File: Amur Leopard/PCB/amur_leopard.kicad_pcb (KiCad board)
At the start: 2 copper layers, 110.3 x 38.1 mm, 32 parts, among them SW1 SW_Push, U1 ATmega32U4-AU, Y1 16MHz

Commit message: Improve Amur Leopard-PCB
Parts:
- moved USB1 28.3 mm to (151.6, 109.5), turned to 0 degrees
- moved R3 24.8 mm to (161.3, 111.6), turned to 270 degrees
- moved R2 21.2 mm to (159.4, 109.7), turned to 270 degrees
- moved C3 1.75 mm to (153.8, 96.0), turned to 270 degrees
- moved C7 0.13 mm to (165.1, 109.4)
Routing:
- net VCC: track 39.0 -> 18.5 mm
- net GND: track 142.3 -> 133.6 mm
- net Net-(C3-Pad1): track 5.98 -> 8.94 mm
- net Net-(R1-Pad2): track 56.4 -> 53.8 mm
- net D-: track 3.88 -> 6.10 mm
- net Net-(R3-Pad1): track 18.3 -> 17.4 mm, vias 0 -> 2
- net Net-(R2-Pad1): track 17.4 -> 18.2 mm, vias 0 -> 2
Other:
- board size 110.3 x 38.1 mm -> 104.1 x 38.1 mm

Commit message: Improve Amur Leopard-PCB & Add Decorations
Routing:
- added copper zone on B.Cu, net GND
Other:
- board text added: "Panthera Pardus Orientalis"
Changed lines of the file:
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@@
   (general
     (thickness 1.6)
-    (drawings 8)
+    (drawings 9)
     (tracks 334)
     (zones 0)
@@
       (rotate (xyz 0 0 0))
     )
+  )
+  (gr_text "Panthera\nPardus\nOrientalis" (at 165.735 96.393) (layer F.SilkS)
+    (effects (font (size 2 2) (thickness 0.3)))
   )
   (gr_arc (start 152.273 81.75625) (end 152.273 79.375) (angle -90) (layer Edge.Cuts) (width 0.05))
@@
   (segment (start 170.00625 102.425) (end 171.01025 102.425) (width 0.254) (layer B.Cu) (net 26))
   (segment (start 171.01025 102.425) (end 171.323 102.11225) (width 0.254) (layer B.Cu) (net 26))
+  (zone (net 1) (net_name GND) (layer B.Cu) (hatch edge 0.508)
+    (connect_pads (clearance 0.508))
+    (min_thickness 0.254)
+    (fill yes (arc_segments 32) (thermal_gap 0.508) (thermal_bridge_width 0.508))
+    (polygon
+      (pts
+        (xy 164.30625 79.375) (xy 177.8 79.375) (xy 177.8 84.93125) (xy 164.30625 84.93125)
+      )
+    )
+  )
+  (zone (net 1) (net_name GND) (layer B.Cu) (hatch edge 0.508)
+    (connect_pads (clearance 0.508))
+    (min_thickness 0.254)
+    (fill yes (arc_segments 32) (thermal_gap 0.508) (thermal_bridge_width 0.508))
+    (polygon
+      (pts
+        (xy 158.75 92.86875) (xy 169.8625 92.86875) (xy 169.8625 103.98125) (xy 158.75 103.98125)
+      )
+    )
+  )
+  (zone (net 1) (net_name GND) (layer B.Cu) (hatch edge 0.508)
+    (connect_pads (clearance 0.508))
+    (min_thickness 0.254)
+    (fill yes (arc_segments 32) (thermal_gap 0.508) (thermal_bridge_width 0.508))
+    (polygon
+      (pts
+        (xy 150.01875 104.775) (xy 157.1625 104.775) (xy 157.1625 114.3) (xy 150.01875 114.3)
+      )
+    )
+  )
 )

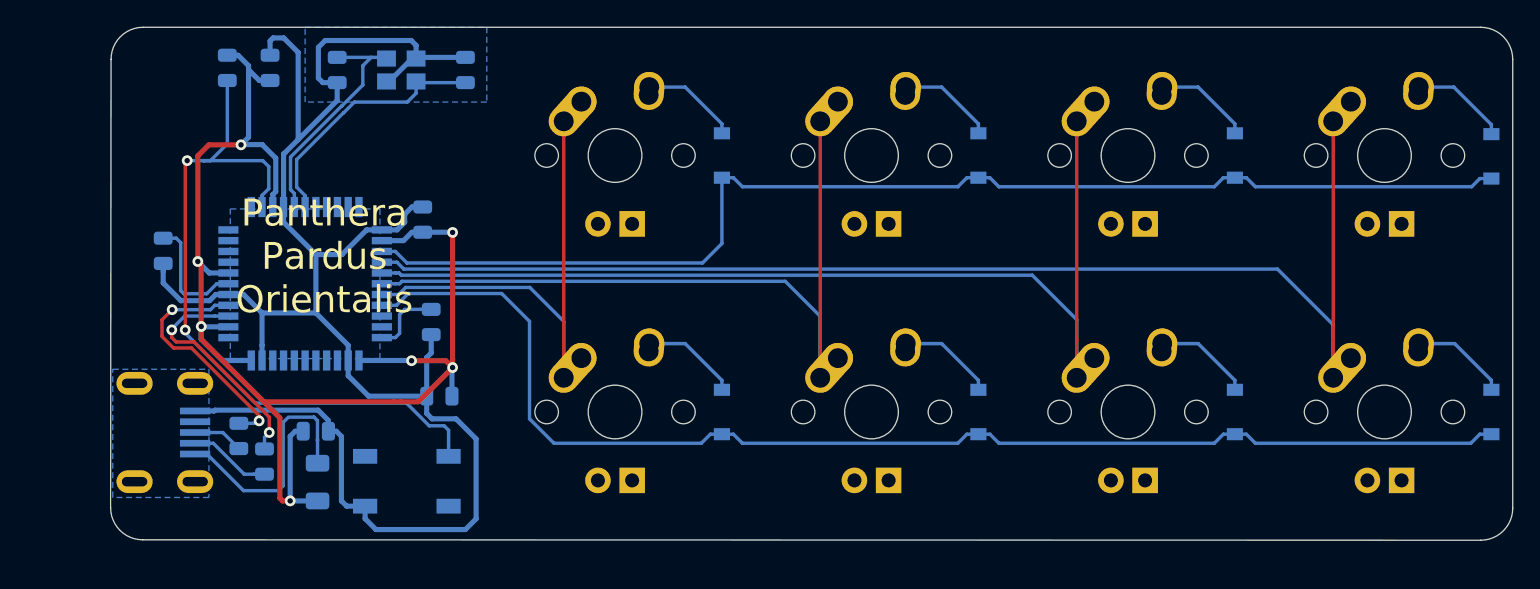
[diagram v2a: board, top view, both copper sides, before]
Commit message: Add MountingHoles to Amur Leopard
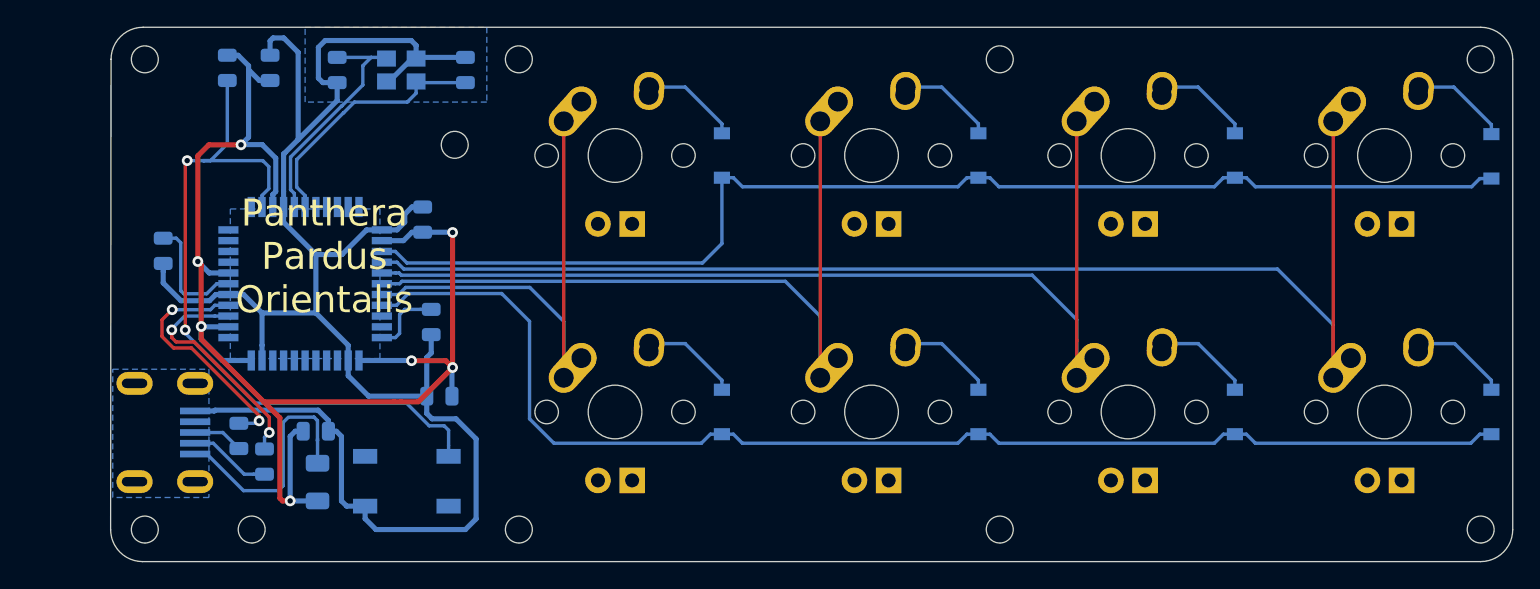
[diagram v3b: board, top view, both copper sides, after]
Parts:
- added H1: MountingHole, MountingHole:MountingHole_2mm, B.Cu at (251.6, 81.8)
- added H10: MountingHole, MountingHole:MountingHole_2mm, B.Cu at (152.4, 116.7)
- added H2: MountingHole, MountingHole:MountingHole_2mm, B.Cu at (251.6, 116.7)
- added H3: MountingHole, MountingHole:MountingHole_2mm, B.Cu at (180.2, 116.7)
- added H4: MountingHole, MountingHole:MountingHole_2mm, B.Cu at (160.3, 116.7)
- added H5: MountingHole, MountingHole:MountingHole_2mm, B.Cu at (152.4, 81.8)
- added H6: MountingHole, MountingHole:MountingHole_2mm, B.Cu at (215.9, 116.7)
- added H7: MountingHole, MountingHole:MountingHole_2mm, B.Cu at (215.9, 81.8)
- added H8: MountingHole, MountingHole:MountingHole_2mm, B.Cu at (175.4, 88.1)
- added H9: MountingHole, MountingHole:MountingHole_2mm, B.Cu at (180.2, 81.8)
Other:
- board size 104.1 x 38.1 mm -> 104.1 x 39.7 mm
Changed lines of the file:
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@@
     (tracks 334)
     (zones 0)
-    (modules 32)
+    (modules 42)
     (nets 49)
   )
@@
     (add_net GND)
   )
+  (module MountingHole:MountingHole_2mm (layer B.Cu)
+    (at 152.4 81.75625)
+    (descr "Mounting Hole 2mm, no annular")
+    (tags "mounting hole 2mm no annular")
+    (attr virtual)
+    (fp_text reference H5 (at 0 3.2) (layer B.SilkS)
+      (effects (font (size 1 1) (thickness 0.15)) (justify mirror))
+    )
+    (fp_text value MountingHole (at 0 -3.1) (layer B.Fab)
+      (effects (font (size 1 1) (thickness 0.15)) (justify mirror))
+    )
+    (fp_circle (center 0 0) (end 2.25 0) (layer B.CrtYd) (width 0.05))
+    (fp_circle (center 0 0) (end 2 0) (layer Cmts.User) (width 0.15))
+    (fp_text user %R (at 0.3 0) (layer B.Fab)
+      (effects (font (size 1 1) (thickness 0.15)) (justify mirror))
+    )
+    (pad "" np_thru_hole circle (at 0 0) (size 2 2) (drill 2) (layers *.Cu *.Mask))
+  )
+  (module MountingHole:MountingHole_2mm (layer B.Cu)
+    (at 160.3375 116.68125)
+    (descr "Mounting Hole 2mm, no annular")
+    (tags "mounting hole 2mm no annular")
+    (attr virtual)
+    (fp_text reference H4 (at 0 3.2) (layer B.SilkS)
+      (effects (font (size 1 1) (thickness 0.15)) (justify mirror))
+    )
+    (fp_text value MountingHole (at 0 -3.1) (layer B.Fab)
+      (effects (font (size 1 1) (thickness 0.15)) (justify mirror))
+    )
+    (fp_circle (center 0 0) (end 2.25 0) (layer B.CrtYd) (width 0.05))
+    (fp_circle (center 0 0) (end 2 0) (layer Cmts.User) (width 0.15))
+    (fp_text user %R (at 0.3 0) (layer B.Fab)
+      (effects (font (size 1 1) (thickness 0.15)) (justify mirror))
+    )
+    (pad "" np_thru_hole circle (at 0 0) (size 2 2) (drill 2) (layers *.Cu *.Mask))
+  )
+  (module MountingHole:MountingHole_2mm (layer B.Cu)
+    (at 175.41875 88.10625)
+    (descr "Mounting Hole 2mm, no annular")
+    (tags "mounting hole 2mm no annular")
+    (attr virtual)
+    (fp_text reference H8 (at 0 3.2) (layer B.SilkS)
+      (effects (font (size 1 1) (thickness 0.15)) (justify mirror))
+    )
+    (fp_text value MountingHole (at 0 -3.1) (layer B.Fab)
+      (effects (font (size 1 1) (thickness 0.15)) (justify mirror))
+    )
+    (fp_text user %R (at 0.3 0) (layer B.Fab)
+      (effects (font (size 1 1) (thickness 0.15)) (justify mirror))
+    )
+    (fp_circle (center 0 0) (end 2 0) (layer Cmts.User) (width 0.15))
+    (fp_circle (center 0 0) (end 2.25 0) (layer B.CrtYd) (width 0.05))
+    (pad "" np_thru_hole circle (at 0 0) (size 2 2) (drill 2) (layers *.Cu *.Mask))
+  )
+  (module MountingHole:MountingHole_2mm (layer B.Cu)
+    (at 152.4 116.68125)
+    (descr "Mounting Hole 2mm, no annular")
+    (tags "mounting hole 2mm no annular")
+    (attr virtual)
+    (fp_text reference H10 (at 0 3.2) (layer B.SilkS)
+      (effects (font (size 1 1) (thickness 0.15)) (justify mirror))
+    )
+    (fp_text value MountingHole (at 0 -3.1) (layer B.Fab)
+      (effects (font (size 1 1) (thickness 0.15)) (justify mirror))
+    )
+    (fp_circle (center 0 0) (end 2.25 0) (layer B.CrtYd) (width 0.05))
+    (fp_circle (center 0 0) (end 2 0) (layer Cmts.User) (width 0.15))
+    (fp_text user %R (at 0.3 0) (layer B.Fab)
+      (effects (font (size 1 1) (thickness 0.15)) (justify mirror))
+    )
+    (pad "" np_thru_hole circle (at 0 0) (size 2 2) (drill 2) (layers *.Cu *.Mask))
+  )
+  (module MountingHole:MountingHole_2mm (layer B.Cu)
+    (at 180.18125 81.75625)
+    (descr "Mounting Hole 2mm, no annular")
+    (tags "mounting hole 2mm no annular")
+    (attr virtual)
+    (fp_text reference H9 (at 0 3.2) (layer B.SilkS)
+      (effects (font (size 1 1) (thickness 0.15)) (justify mirror))
+    )
+    (fp_text value MountingHole (at 0 -3.1) (layer B.Fab)
+      (effects (font (size 1 1) (thickness 0.15)) (justify mirror))
+    )
+    (fp_circle (center 0 0) (end 2.25 0) (layer B.CrtYd) (width 0.05))
+    (fp_circle (center 0 0) (end 2 0) (layer Cmts.User) (width 0.15))
+    (fp_text user %R (at 0.3 0) (layer B.Fab)
+      (effects (font (size 1 1) (thickness 0.15)) (justify mirror))
+    )
+    (pad "" np_thru_hole circle (at 0 0) (size 2 2) (drill 2) (layers *.Cu *.Mask))
+  )
+  (module MountingHole:MountingHole_2mm (layer B.Cu)
+    (at 215.9 81.75625)
+    (descr "Mounting Hole 2mm, no annular")
+    (tags "mounting hole 2mm no annular")
+    (attr virtual)
+    (fp_text reference H7 (at 0 3.2) (layer B.SilkS)
+      (effects (font (size 1 1) (thickness 0.15)) (justify mirror))
+    )
+    (fp_text value MountingHole (at 0 -3.1) (layer B.Fab)
+      (effects (font (size 1 1) (thickness 0.15)) (justify mirror))
+    )
+    (fp_text user %R (at 0.3 0) (layer B.Fab)
+      (effects (font (size 1 1) (thickness 0.15)) (justify mirror))
+    )
+    (fp_circle (center 0 0) (end 2 0) (layer Cmts.User) (width 0.15))
+    (fp_circle (center 0 0) (end 2.25 0) (layer B.CrtYd) (width 0.05))
+    (pad "" np_thru_hole circle (at 0 0) (size 2 2) (drill 2) (layers *.Cu *.Mask))
+  )
+  (module MountingHole:MountingHole_2mm (layer B.Cu)
+    (at 215.9 116.68125)
+    (descr "Mounting Hole 2mm, no annular")
+    (tags "mounting hole 2mm no annular")
+    (attr virtual)
+    (fp_text reference H6 (at 0 3.2) (layer B.SilkS)
+      (effects (font (size 1 1) (thickness 0.15)) (justify mirror))
+    )
+    (fp_text value MountingHole (at 0 -3.1) (layer B.Fab)
+      (effects (font (size 1 1) (thickness 0.15)) (justify mirror))
+    )
+    (fp_circle (center 0 0) (end 2.25 0) (layer B.CrtYd) (width 0.05))
+    (fp_circle (center 0 0) (end 2 0) (layer Cmts.User) (width 0.15))
+    (fp_text user %R (at 0.3 0) (layer B.Fab)
+      (effects (font (size 1 1) (thickness 0.15)) (justify mirror))
+    )
+    (pad "" np_thru_hole circle (at 0 0) (size 2 2) (drill 2) (layers *.Cu *.Mask))
+  )
+  (module MountingHole:MountingHole_2mm (layer B.Cu)
+    (at 180.18125 116.68125)
+    (descr "Mounting Hole 2mm, no annular")
+    (tags "mounting hole 2mm no annular")
+    (attr virtual)
+    (fp_text reference H3 (at 0 3.2) (layer B.SilkS)
+      (effects (font (size 1 1) (thickness 0.15)) (justify mirror))
+    )
+    (fp_text value MountingHole (at 0 -3.1) (layer B.Fab)
+      (effects (font (size 1 1) (thickness 0.15)) (justify mirror))
+    )
+    (fp_circle (center 0 0) (end 2.25 0) (layer B.CrtYd) (width 0.05))
+    (fp_circle (center 0 0) (end 2 0) (layer Cmts.User) (width 0.15))
+    (fp_text user %R (at 0.3 0) (layer B.Fab)
+      (effects (font (size 1 1) (thickness 0.15)) (justify mirror))
+    )
+    (pad "" np_thru_hole circle (at 0 0) (size 2 2) (drill 2) (layers *.Cu *.Mask))
+  )
+  (module MountingHole:MountingHole_2mm (layer B.Cu)
+    (at 251.61875 116.68125)
+    (descr "Mounting Hole 2mm, no annular")
+    (tags "mounting hole 2mm no annular")
+    (attr virtual)
+    (fp_text reference H2 (at 0 3.2) (layer B.SilkS)
+      (effects (font (size 1 1) (thickness 0.15)) (justify mirror))
+    )
+    (fp_text value MountingHole (at 0 -3.1) (layer B.Fab)
+      (effects (font (size 1 1) (thickness 0.15)) (justify mirror))
+    )
+    (fp_circle (center 0 0) (end 2.25 0) (layer B.CrtYd) (width 0.05))
+    (fp_circle (center 0 0) (end 2 0) (layer Cmts.User) (width 0.15))
+    (fp_text user %R (at 0.3 0) (layer B.Fab)
+      (effects (font (size 1 1) (thickness 0.15)) (justify mirror))
+    )
+    (pad "" np_thru_hole circle (at 0 0) (size 2 2) (drill 2) (layers *.Cu *.Mask))
+  )
+  (module MountingHole:MountingHole_2mm (layer B.Cu)
+    (at 251.61875 81.75625)
+    (descr "Mounting Hole 2mm, no annular")
+    (tags "mounting hole 2mm no annular")
+    (attr virtual)
+    (fp_text reference H1 (at 0 3.2) (layer B.SilkS)
+      (effects (font (size 1 1) (thickness 0.15)) (justify mirror))
+    )
+    (fp_text value MountingHole (at 0 -3.1) (layer B.Fab)
+      (effects (font (size 1 1) (thickness 0.15)) (justify mirror))
+    )
+    (fp_circle (center 0 0) (end 2.25 0) (layer B.CrtYd) (width 0.05))
+    (fp_circle (center 0 0) (end 2 0) (layer Cmts.User) (width 0.15))
+    (fp_text user %R (at 0.3 0) (layer B.Fab)
+      (effects (font (size 1 1) (thickness 0.15)) (justify mirror))
+    )
+    (pad "" np_thru_hole circle (at 0 0) (size 2 2) (drill 2) (layers *.Cu *.Mask))
+  )
   (module MX_Alps_Hybrid:MX-1U (layer F.Cu)
     (at 244.475 107.95)
@@
     )
   )
+  (gr_arc (start 152.273 81.75625) (end 152.273 79.375) (angle -90) (layer Edge.Cuts) (width 0.05))
   (gr_text "Panthera\nPardus\nOrientalis" (at 165.735 96.393) (layer F.SilkS)
     (effects (font (size 2 2) (thickness 0.3)))
   )
-  (gr_arc (start 152.273 81.75625) (end 152.273 79.375) (angle -90) (layer Edge.Cuts) (width 0.05))
-  (gr_line (start 149.89175 81.75625) (end 149.86 115.062) (layer Edge.Cuts) (width 0.05))
-  (gr_arc (start 152.24125 115.062) (end 149.86 115.062) (angle -90) (layer Edge.Cuts) (width 0.05))
-  (gr_line (start 251.61875 117.475) (end 152.24125 117.44325) (layer Edge.Cuts) (width 0.05))
+  (gr_line (start 149.89175 81.75625) (end 149.86 116.68125) (layer Edge.Cuts) (width 0.05))
+  (gr_arc (start 152.24125 116.68125) (end 149.86 116.68125) (angle -90) (layer Edge.Cuts) (width 0.05))
+  (gr_line (start 251.61875 119.0625) (end 152.24125 119.0625) (layer Edge.Cuts) (width 0.05))
   (gr_line (start 251.61875 79.375) (end 152.273 79.375) (layer Edge.Cuts) (width 0.05))
-  (gr_line (start 254 115.09375) (end 254 81.75625) (layer Edge.Cuts) (width 0.05))
-  (gr_arc (start 251.61875 115.09375) (end 251.61875 117.475) (angle -90) (layer Edge.Cuts) (width 0.05))
+  (gr_line (start 254 116.68125) (end 254 81.75625) (layer Edge.Cuts) (width 0.05))
+  (gr_arc (start 251.61875 116.68125) (end 251.61875 119.0625) (angle -90) (layer Edge.Cuts) (width 0.05))
   (gr_arc (start 251.61875 81.75625) (end 254 81.75625) (angle -90) (layer Edge.Cuts) (width 0.05))
   (segment (start 172.247098 81.7) (end 172.55 81.7) (width 0.381) (layer B.Cu) (net 1))
